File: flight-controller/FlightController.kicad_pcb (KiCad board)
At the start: 2 copper layers, 57 x 37 mm, 43 parts, among them J1 MSD-4-A, J10 GT-USB-7010B, J2 Conn_01x03_Pin, J3 Conn_01x03_Pin, J4 Conn_01x03_Pin, J5 Conn_01x03_Pin, J6 Conn_01x04_Pin, J7 Conn_01x03_Pin, J8 Conn_01x03_Pin, J9 Conn_01x04_Pin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

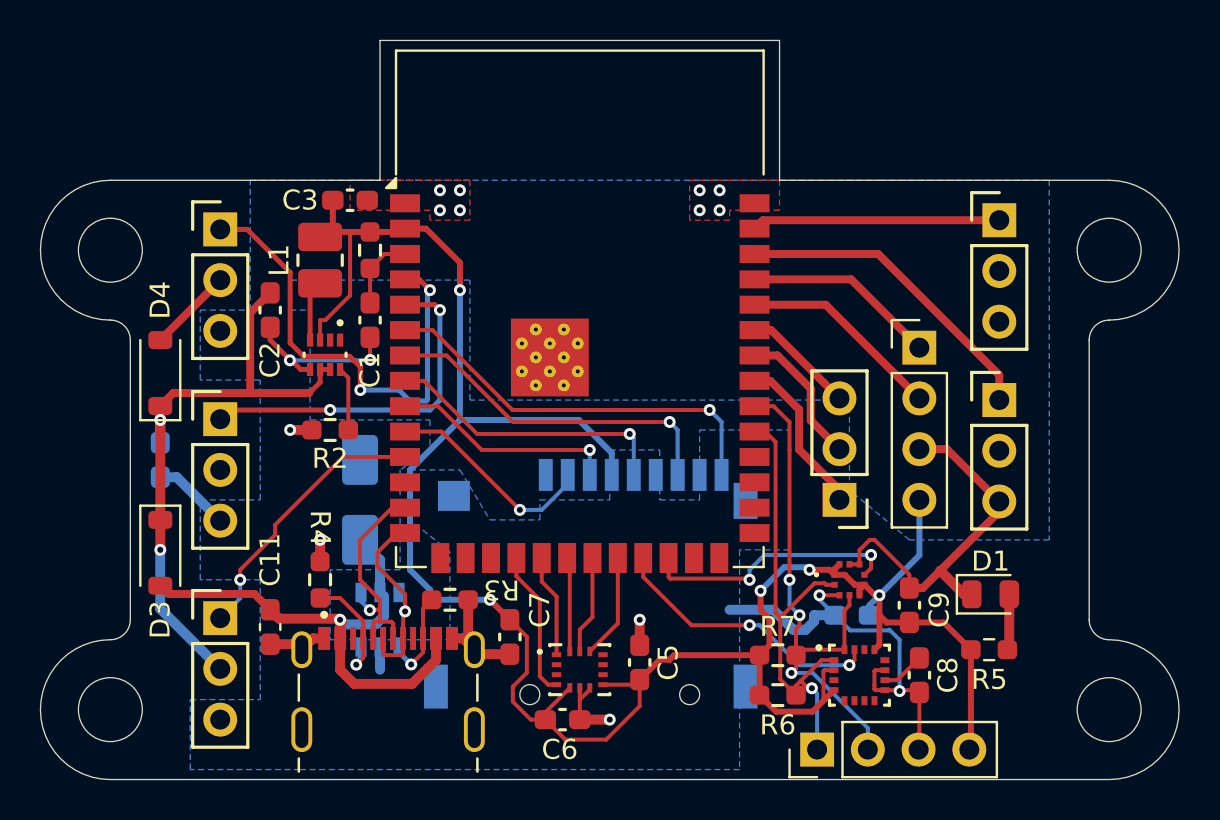
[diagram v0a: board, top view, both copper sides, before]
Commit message: 4 layerify board
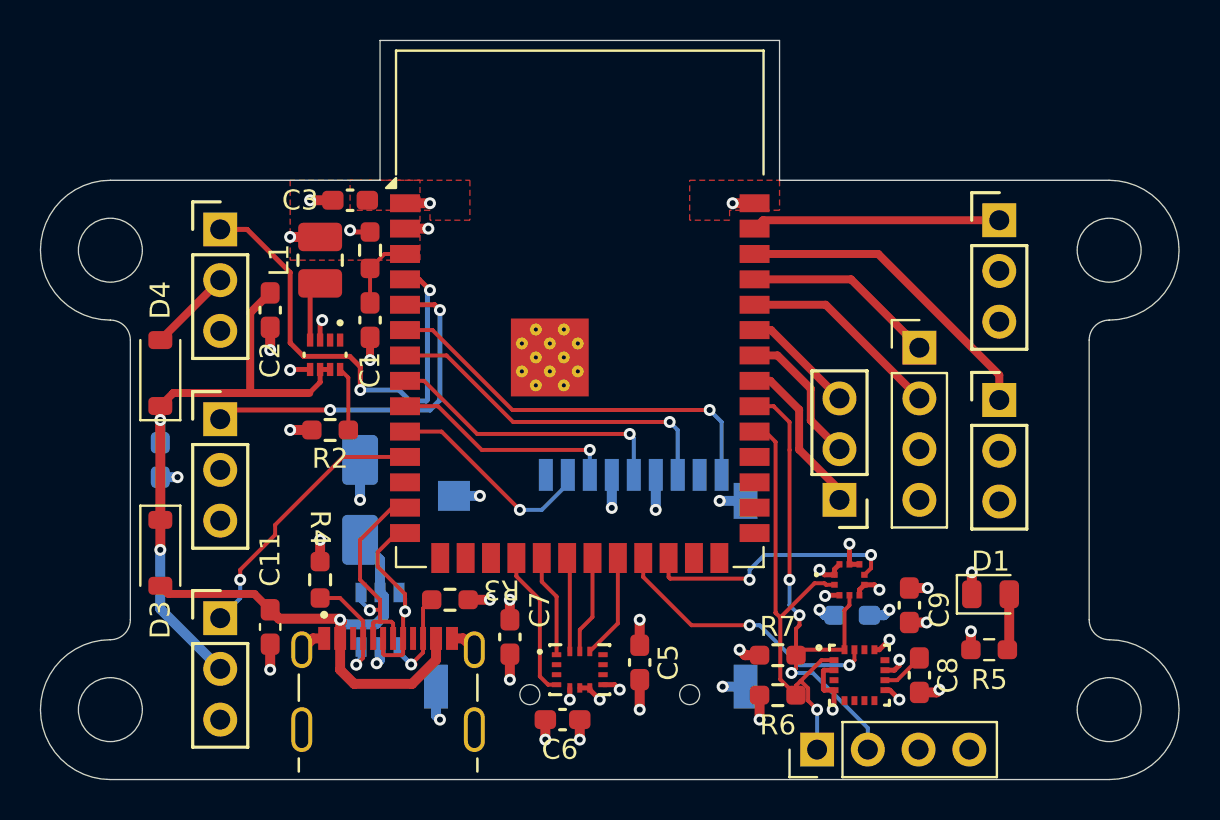
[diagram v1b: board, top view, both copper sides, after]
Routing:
- net +3.3V: track 111.8 -> 24.7 mm, vias 5 -> 20
- net GND: track 70.4 -> 37.0 mm, vias 16 -> 29
- added copper zone on F.Cu, net +3.3V
- added copper zone on In2.Cu, net +3.3V
- added copper zone on In1.Cu, net GND
- removed copper zone on B.Cu, net GND
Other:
- copper layers 2 -> 4
